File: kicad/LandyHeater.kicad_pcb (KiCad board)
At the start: 4 copper layers, 80 x 50 mm, 139 parts, among them J1 12V IN, J2 AUTOTERM, J3 1-Wire, J4 Taster/LED, J5 USB4105-GF-A-060, Q1 2N7002K, SW1 RESET, SW2 BOOT, SW3 DIAG, U1 TPD2EUSB30DRTR, U2 TPS259470LRPWR, U3 LMR43620MSC3RPERQ1, U4 ESP32-S3-WROOM-1U-N16R8, U5 TPS3808G33DBVR, U6 RV-8263-C8, U7 TXU0202QDCURQ1, U8 TPS22945DCKR, U9 BCR421UW6Q-7

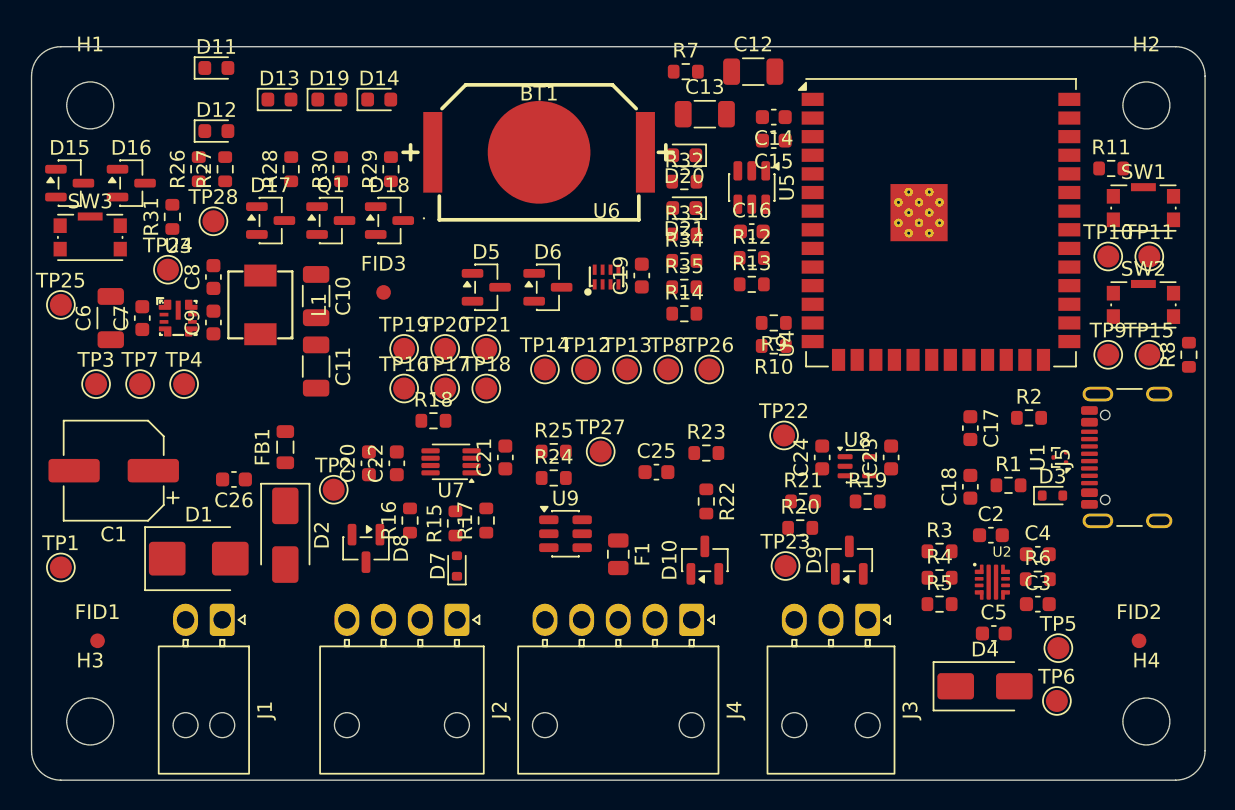
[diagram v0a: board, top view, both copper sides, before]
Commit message: Step 6.1: silkscreen per E-02 and Y-08
- tools/silkscreen.py: references to F.Fab; connector names, RST/BOOT/DIAG,
  status LEDs, G-01 energy-flow diagram, 28 test point names, revision
- Battery clip footprint: polarity marks moved above the clips (no longer
  on the D20 pad)
- TP24 next to TP25 so DIAG/GND can be bridged (G-03); TP11/TP15 nudged
  0.5/0.2 mm to fit 0.8 mm labels; fiducial keepout creation made repeatable
- DRC: no violations or warnings apart from unrouted connections

Co-Authored-By: Claude Opus 5.5 <noreply@anthropic.com>
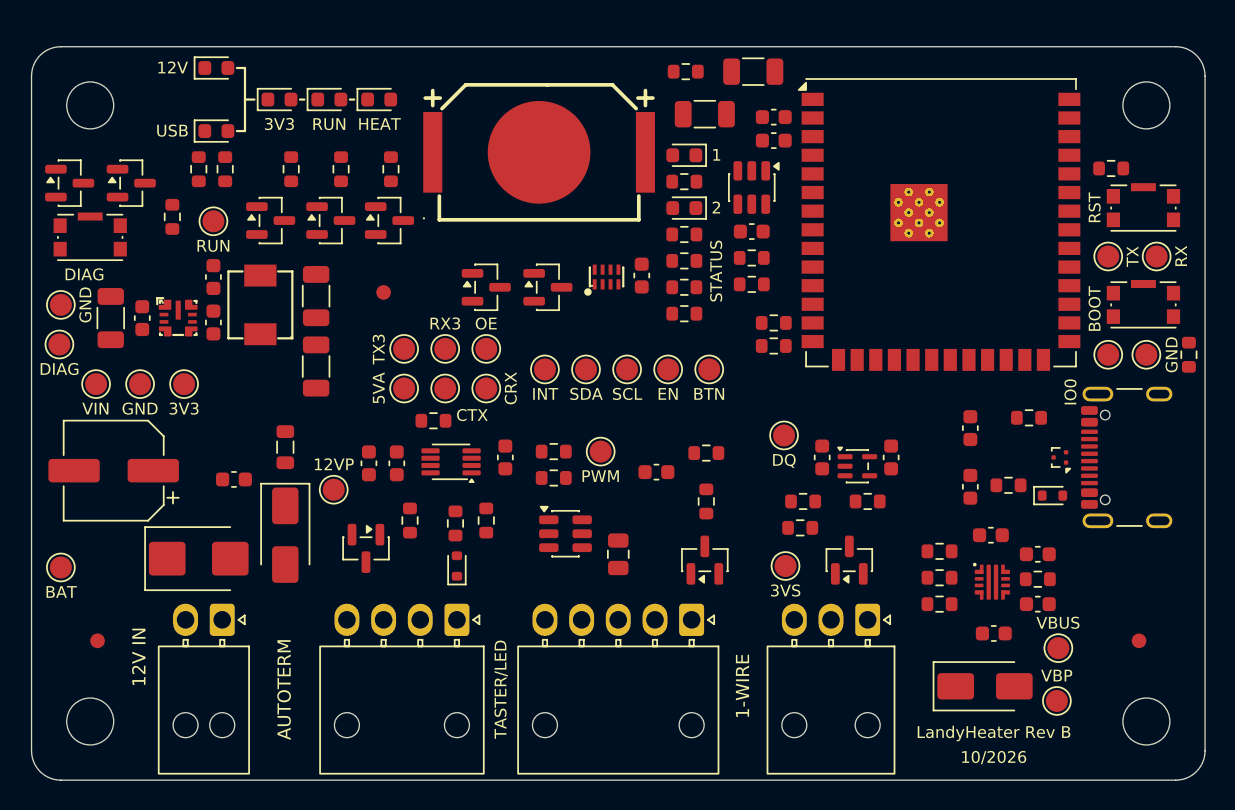
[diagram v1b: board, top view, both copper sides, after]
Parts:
- moved TP24 8.99 mm to (101.9, 120.3)
- moved TP11 0.50 mm to (176.7, 114.3)
- moved TP15 0.20 mm to (176.0, 121.0)
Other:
- board text added: "1"
- board text added: "1-WIRE"
- board text added: "10/2026"
- board text added: "12V"
- board text added: "12V IN"
- board text added: "12VP"
- board text added: "2"
- board text added: "3V3"
- board text added: "3VS"
- board text added: "5VA"
- board text added: "AUTOTERM"
- board text added: "BAT"
- board text added: "BOOT"
- board text added: "BTN"
- board text added: "CRX"
- board text added: "CTX"
- board text added: "DIAG"
- board text added: "DQ"
- board text added: "EN"
- board text added: "GND"
- board text added: "HEAT"
- board text added: "INT"
- board text added: "IO0"
- board text added: "LandyHeater Rev B"
- board text added: "OE"
- board text added: "PWM"
- board text added: "RST"
- board text added: "RUN"
- board text added: "RX"
- board text added: "RX3"
- board text added: "SCL"
- board text added: "SDA"
- board text added: "STATUS"
- board text added: "TASTER/LED"
- board text added: "TX"
- board text added: "TX3"
- board text added: "USB"
- board text added: "VBP"
- board text added: "VBUS"
- board text added: "VIN"

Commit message: Step 6.2: copper zones (L2 GND, L3 split VIN_SYS/3V3, L1/L4 GND pours)
- tools/zones.py; outer-layer pours stay unfilled until routing is done
- Fix polygon ownership (thisown) in zone and keepout creation: Python freed
  the polygon passed to ZONE.SetOutline, crashing the zone filler

Co-Authored-By: Claude Opus 5.5 <noreply@anthropic.com>
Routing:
- added copper zone on In2.Cu, net 3V3_CORE
- added copper zone on B.Cu, net GND
- added copper zone on F.Cu, net GND
- added copper zone on In1.Cu, net GND
- added copper zone on In2.Cu, net VIN_SYS
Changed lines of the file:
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@@
 	(layers
 		(0 "F.Cu" signal)
-		(4 "In1.Cu" signal)
-		(6 "In2.Cu" signal)
+		(4 "In1.Cu" power)
+		(6 "In2.Cu" mixed)
 		(2 "B.Cu" signal)
 		(9 "F.Adhes" user "F.Adhesive")
@@
 	)
 	(zone
+		(net "GND")
+		(layer "F.Cu")
+		(name "GND L1")
+		(hatch edge 0.5)
+		(connect_pads
+			(clearance 0.25)
+		)
+		(min_thickness 0.2)
+		(fill yes
+			(thermal_gap 0.3)
+			(thermal_bridge_width 0.4)
+			(island_removal_mode 0)
+		)
+		(polygon
+			(pts
+				(xy 100.3 100.3) (xy 179.7 100.3) (xy 179.7 149.7) (xy 100.3 149.7)
+			)
+		)
+	)
+	(zone
 		(layers "F.Cu" "B.Cu" "In1.Cu" "In2.Cu")
 		(name "Sperrfläche FID1")
@@
 			)
 		)
+	)
+	(zone
+		(net "GND")
+		(layer "B.Cu")
+		(name "GND L4")
+		(hatch edge 0.5)
+		(connect_pads
+			(clearance 0.25)
+		)
+		(min_thickness 0.2)
+		(fill yes
+			(thermal_gap 0.3)
+			(thermal_bridge_width 0.4)
+			(island_removal_mode 0)
+		)
+		(polygon
+			(pts
+				(xy 100.3 100.3) (xy 179.7 100.3) (xy 179.7 149.7) (xy 100.3 149.7)
+			)
+		)
+	)
+	(zone
+		(net "GND")
+		(layer "In1.Cu")
+		(name "GND L2")
+		(hatch edge 0.5)
+		(connect_pads
+			(clearance 0.2)
+		)
+		(min_thickness 0.2)
+		(fill yes
+			(thermal_gap 0.3)
+			(thermal_bridge_width 0.4)
+			(island_removal_mode 0)
+		)
+		(polygon
+			(pts
+				(xy 100.3 100.3) (xy 179.7 100.3) (xy 179.7 149.7) (xy 100.3 149.7)
+			)
+		)
+	)
+	(zone
+		(net "VIN_SYS")
+		(layer "In2.Cu")
+		(name "VIN_SYS L3")
+		(hatch edge 0.5)
+		(priority 1)
+		(connect_pads
+			(clearance 0.2)
+		)
+		(min_thickness 0.2)
+		(fill yes
+			(thermal_gap 0.3)
+			(thermal_bridge_width 0.4)
+			(island_removal_mode 0)
+		)
+		(polygon
+			(pts
+				(xy 100.3 116) (xy 109.3 116) (xy 109.3 124.6) (xy 121 124.6) (xy 121 131) (xy 179.7 131) (xy 179.7 149.7)
+				(xy 100.3 149.7)
+			)
+		)
+	)
+	(zone
+		(net "3V3_CORE")
+		(layer "In2.Cu")
+		(name "3V3 L3")
+		(hatch edge 0.5)
+		(priority 1)
+		(connect_pads
+			(clearance 0.2)
+		)
+		(min_thickness 0.2)
+		(fill yes
+			(thermal_gap 0.3)
+			(thermal_bridge_width 0.4)
+			(island_removal_mode 0)
+		)
+		(polygon
+			(pts
+				(xy 100.3 100.3) (xy 179.7 100.3) (xy 179.7 130.6) (xy 121.4 130.6) (xy 121.4 124.2) (xy 109.7 124.2)
+				(xy 109.7 115.6) (xy 100.3 115.6)
+			)
+		)
